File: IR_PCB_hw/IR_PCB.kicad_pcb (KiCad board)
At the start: 4 copper layers, 49.5 x 49 mm, 130 parts, among them Q1 M28S, Q10 SI2303, Q11 SI2303, Q2 M28S, Q3 TSOP48xx, Q4 TSOP48xx, Q5 SI2303, Q6 TSOP48xx, Q7 SI2303, Q8 SI2303, Q9 SI2303

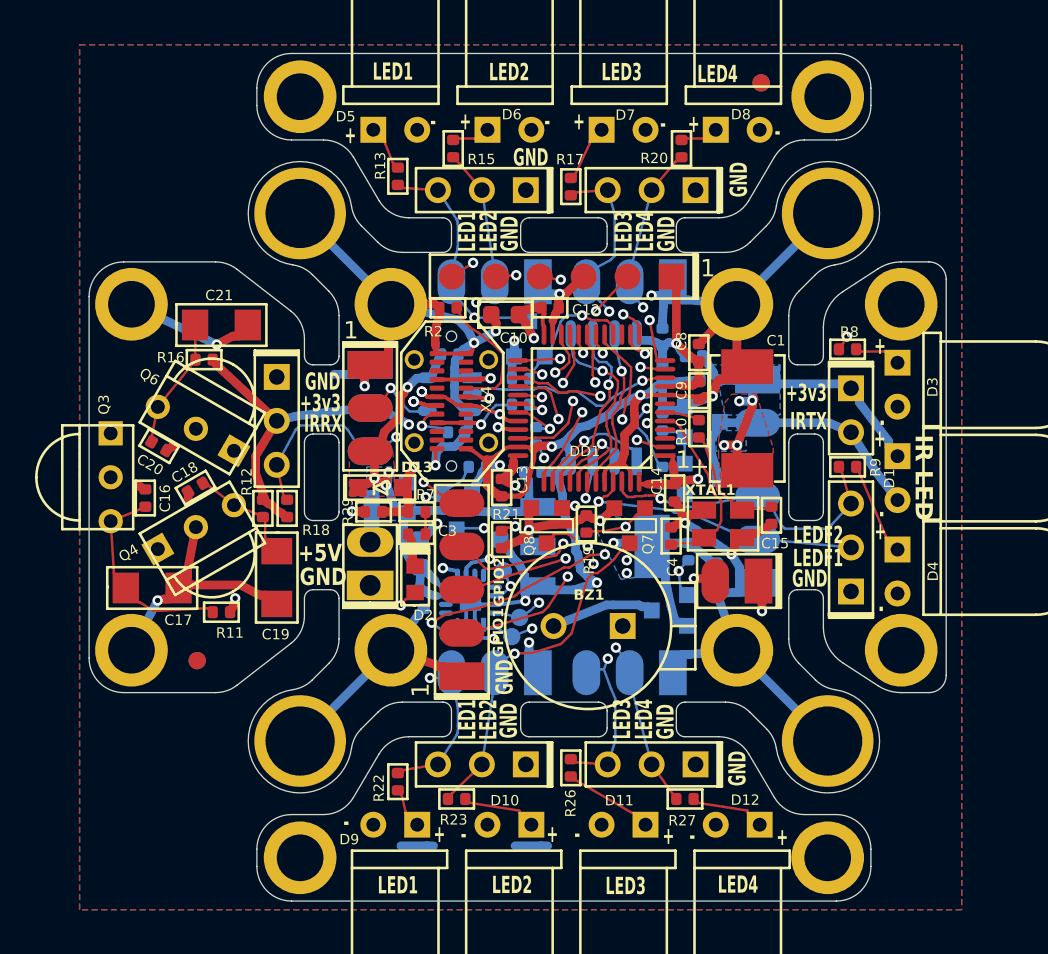
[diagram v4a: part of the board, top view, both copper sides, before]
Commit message: Replace USB conn with micro one Replace 0402 wit 0603
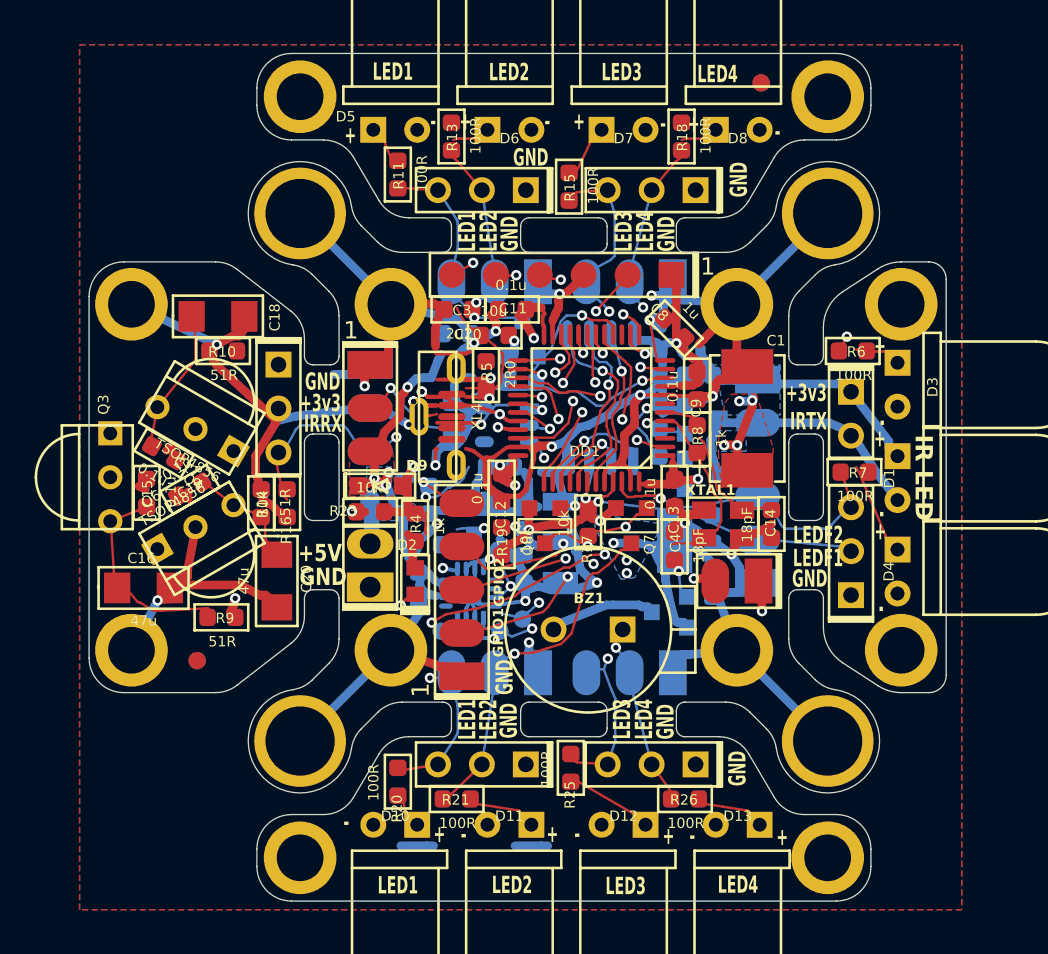
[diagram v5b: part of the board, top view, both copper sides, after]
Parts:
- removed the C15 at (152.0, 111.2)
- removed the C17 at (116.2, 115.4)
- removed the C21 at (120.2, 100.2)
- removed the C23 at (131.7, 113.4)
- removed C26: 10u, Capacitors:CAP_0603_Fab
- removed the D9 at (130.2, 129.1)
- removed the R2 at (133.3, 99.2)
- removed the R3 at (133.8, 106.4)
- added C14: 18pF, Capacitors:CAP_0603_Silks, F.Cu at (152.0, 111.7)
- added C16: 47u, Capacitors:CAP_1206, F.Cu at (115.7, 115.4)
- added C20: 47u, Capacitors:CAP_1206, F.Cu at (123.4, 115.0)
- added C22: 10u, Capacitors:CAP_0603_Silks, B.Cu at (132.1, 112.9)
- added C24: 10u, Capacitors:CAP_0603_Silks, B.Cu at (132.2, 110.3)
- added D13: ~, LEDs:LED5mmR, F.Cu at (150.1, 129.1)
- BZ1: value PS-9627 -> 9650-5.5R/16R
- C1: value 470uF -> 330uF
- C10, C25: footprint Capacitors:CAP_0603_Fab -> Capacitors:CAP_0603_Silks
- C11: renamed from C12; footprint Capacitors:CAP_0402_Fab -> Capacitors:CAP_0603_Silks
- C12: renamed from C13; footprint Capacitors:CAP_0402_Fab -> Capacitors:CAP_0603_Silks
- C13: renamed from C14; footprint Capacitors:CAP_0402_Fab -> Capacitors:CAP_0603_Silks
- C15: renamed from C16; footprint Capacitors:CAP_0402_Fab -> Capacitors:CAP_0603_Silks
- C17: renamed from C18; footprint Capacitors:CAP_0402_Fab -> Capacitors:CAP_0603_Silks
- C19: renamed from C20; footprint Capacitors:CAP_0402_Fab -> Capacitors:CAP_0603_Silks
- C2, C3, C4, C5, C6, C7, C8, C9: footprint Capacitors:CAP_0402_Fab -> Capacitors:CAP_0603_Silks
- C21: renamed from C22; footprint Capacitors:CAP_0402_Fab -> Capacitors:CAP_0603_Silks
- C23: renamed from C24; footprint Capacitors:CAP_0402_Fab -> Capacitors:CAP_0603_Silks
- D10, D11, D12, D5, D6, D7, D8: value BL-L502URC -> ~
- D2: value L-C191LBCT -> LTST-C191KGKT
- D3, D4: value BL-L522PGC -> ~
- DD2: value W25Q32JV -> W25Q32JVSIQ
- Q10: renamed from Q9; value SI2303 -> SI2301
- Q11, Q5, Q7, Q8: value SI2303 -> SI2301
- Q3, Q4, Q6: value TSOP48xx -> TSOP4856
- Q9: renamed from Q10; value SI2303 -> SI2301
- R1: footprint Resistors:RES_0402_Fab -> Resistors:RES_0603_Silks
- R10: renamed from R12; footprint Resistors:RES_0402_Fab -> Resistors:RES_0603_Silks
- R11: renamed from R13; footprint Resistors:RES_0402_Fab -> Resistors:RES_0603_Silks
- R12: renamed from R14; footprint Resistors:RES_0402_Fab -> Resistors:RES_0603_Silks
- R13: renamed from R15; footprint Resistors:RES_0402_Fab -> Resistors:RES_0603_Silks
- R14: renamed from R16; footprint Resistors:RES_0402_Fab -> Resistors:RES_0603_Silks
- R15: renamed from R17; footprint Resistors:RES_0402_Fab -> Resistors:RES_0603_Silks
- R16: renamed from R18; footprint Resistors:RES_0402_Fab -> Resistors:RES_0603_Silks
- R17: renamed from R19; footprint Resistors:RES_0402_Fab -> Resistors:RES_0603_Silks
- R18: renamed from R20; footprint Resistors:RES_0402_Fab -> Resistors:RES_0603_Silks
- R19: renamed from R21; footprint Resistors:RES_0402_Fab -> Resistors:RES_0603_Silks
- R2: renamed from R4; footprint Resistors:RES_0402_Fab -> Resistors:RES_0603_Silks
- R20: renamed from R22; footprint Resistors:RES_0402_Fab -> Resistors:RES_0603_Silks
- R21: renamed from R23; footprint Resistors:RES_0402_Fab -> Resistors:RES_0603_Silks
- R22: renamed from R24; footprint Resistors:RES_0402_Fab -> Resistors:RES_0603_Silks
- R23: renamed from R29; footprint Resistors:RES_0402_Fab -> Resistors:RES_0603_Silks
- R24: renamed from R25; footprint Resistors:RES_0402_Fab -> Resistors:RES_0603_Silks
- R25: renamed from R26; footprint Resistors:RES_0402_Fab -> Resistors:RES_0603_Silks
- R26: renamed from R27; footprint Resistors:RES_0402_Fab -> Resistors:RES_0603_Silks
- R3: renamed from R5; footprint Resistors:RES_0402_Fab -> Resistors:RES_0603_Silks
- R4: renamed from R6; footprint Resistors:RES_0402_Fab -> Resistors:RES_0603_Silks; moved to F.Cu
- R5: renamed from R7; footprint Resistors:RES_0402_Fab -> Resistors:RES_0603_Silks
- R6: renamed from R8; footprint Resistors:RES_0402_Fab -> Resistors:RES_0603_Silks
- R7: renamed from R9; footprint Resistors:RES_0402_Fab -> Resistors:RES_0603_Silks
- R8: renamed from R10; footprint Resistors:RES_0402_Fab -> Resistors:RES_0603_Silks
- R9: renamed from R11; footprint Resistors:RES_0402_Fab -> Resistors:RES_0603_Silks
- XL4: value USB_C -> DS1105-11; footprint Connectors:USBC_24PF-009 -> Connectors:USBmicro_Connfly_DS1105-11
- moved C18 15.5 mm to (120.0, 99.7), turned to 0 degrees
- moved C3 13.2 mm to (133.9, 99.3), turned to 0 degrees
- moved R10 9.39 mm to (120.3, 101.7), turned to 0 degrees
- moved R14 8.93 mm to (122.5, 110.5), turned to 90 degrees
- moved R5 8.85 mm to (135.5, 103.1), turned to 90 degrees
- moved R4 8.78 mm to (131.4, 111.9)
- moved D12 6.60 mm to (143.4, 129.1)
- moved D10 6.60 mm to (130.2, 129.1)
- moved D11 6.60 mm to (136.8, 129.1)
- moved Q6 5.68 mm to (118.7, 111.9), turned to 30 degrees
- moved Q4 5.67 mm to (118.7, 106.2), turned to 150 degrees
- moved R1 4.24 mm to (148.6, 112.0)
- moved R3 4.06 mm to (133.5, 105.5), turned to 90 degrees
- moved DA1 3.76 mm to (136.7, 106.0)
- moved C19 3.07 mm to (118.4, 109.7), turned to -150 degrees
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- renumbered C19 to C18, D13 to D9, TP2 to TP1, TP3 to TP2, TP4 to TP3, TP5 to TP4, XL14 to XL10, XL15 to XL11, XL16 to XL12, XL17 to XL13, XL18 to XL14, XL19 to XL15, XL20 to XL16, XL21 to XL17, XL22 to XL18, XL23 to XL19, XL24 to XL20, XL7 to XL6, XL8 to XL7, XL9 to XL8, XL10 to XL9
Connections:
- C25 pad 1: +PwrUnst -> +3v3
- R20 pad 2: Net-(D9-PadA) -> Net-(D10-PadA)
- R21 pad 2: Net-(D10-PadA) -> Net-(D11-PadA)
- R25 pad 2: Net-(D11-PadA) -> Net-(D12-PadA)
- R26 pad 2: Net-(D12-PadA) -> Net-(D13-PadA)
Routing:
- net (no net): track 0.00 -> 17.4 mm, vias 0 -> 1
- net Net-(D2-PadA): track 14.1 -> 1.93 mm, vias 2 -> 0
- net GND: track 281.7 -> 293.8 mm, vias 19 -> 21
- net /USB_CC1: track 7.66 -> 0.00 mm
- net Net-(C14-Pad1): track 6.89 -> 0.00 mm
- net Net-(D13-PadA): track 0.00 -> 4.33 mm
- net /USB_CC2: track 2.83 -> 0.00 mm, vias 1 -> 0
- net Net-(D9-PadA): track 2.37 -> 0.00 mm
- net Net-(D10-PadA): track 4.33 -> 2.37 mm
- net Net-(Q6-Vs): track 7.55 -> 6.30 mm
- net Net-(Q4-Vs): track 6.30 -> 7.55 mm
- net Net-(D12-PadA): track 4.33 -> 5.18 mm
- net Net-(D11-PadA): track 5.18 -> 4.33 mm

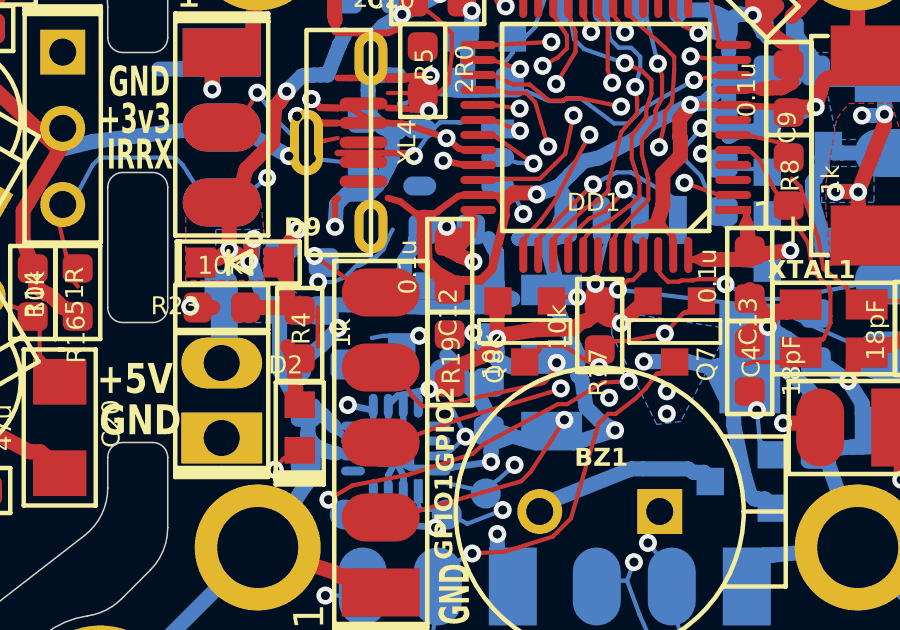
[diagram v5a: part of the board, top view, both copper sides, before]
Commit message: RTOS, UART, XTAL work
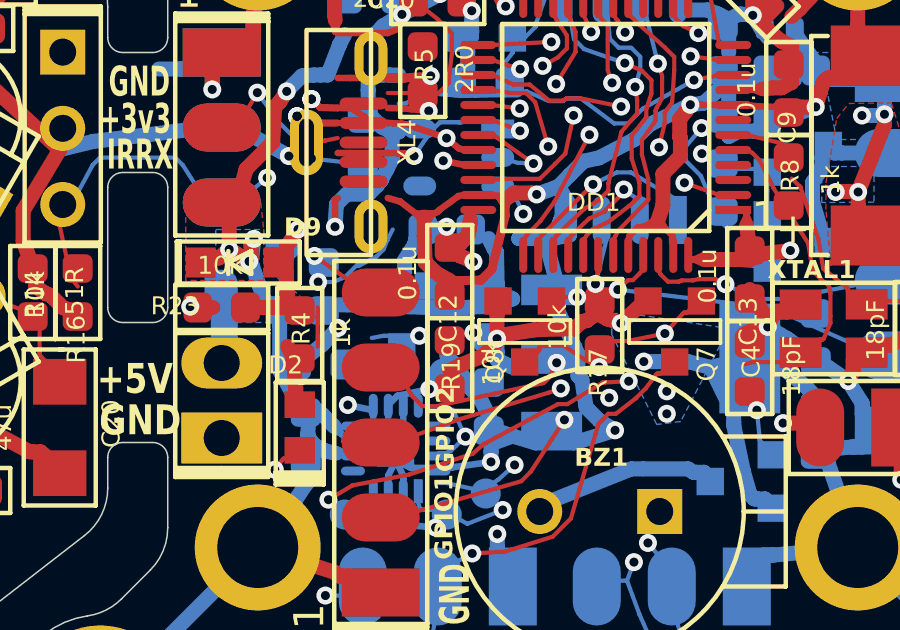
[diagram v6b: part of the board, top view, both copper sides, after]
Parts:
- moved C12 0.20 mm to (136.4, 109.8)
- moved R19 0.20 mm to (136.4, 112.9)
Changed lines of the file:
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@@
   )
   (footprint "Capacitors:CAP_0603_Silks" (layer "F.Cu")
-    (at 136.4 109.6 -90)
+    (at 136.4 109.8 -90)
     (property "Description" "X5R or X7R capacitor, 6.3V or higher")
     (property "Dielectric" "X5R or X7R")
@@
   )
   (footprint "Resistors:RES_0603_Silks" (layer "F.Cu")
-    (at 136.4 112.7 90)
+    (at 136.4 112.9 90)
     (property "Description" "1% resistor")
     (property "PN" "-")

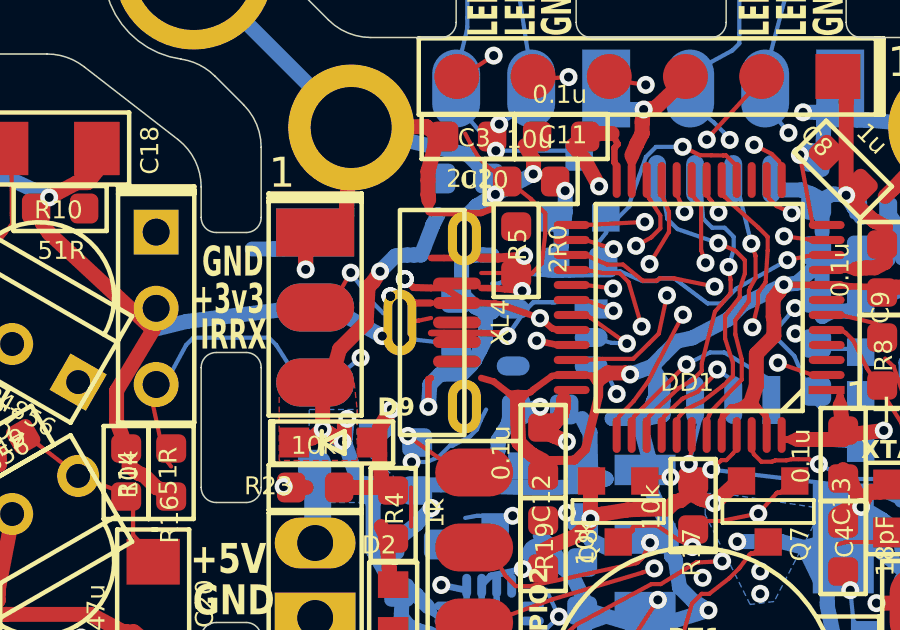
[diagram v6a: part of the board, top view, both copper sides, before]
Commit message: Usb conn moved
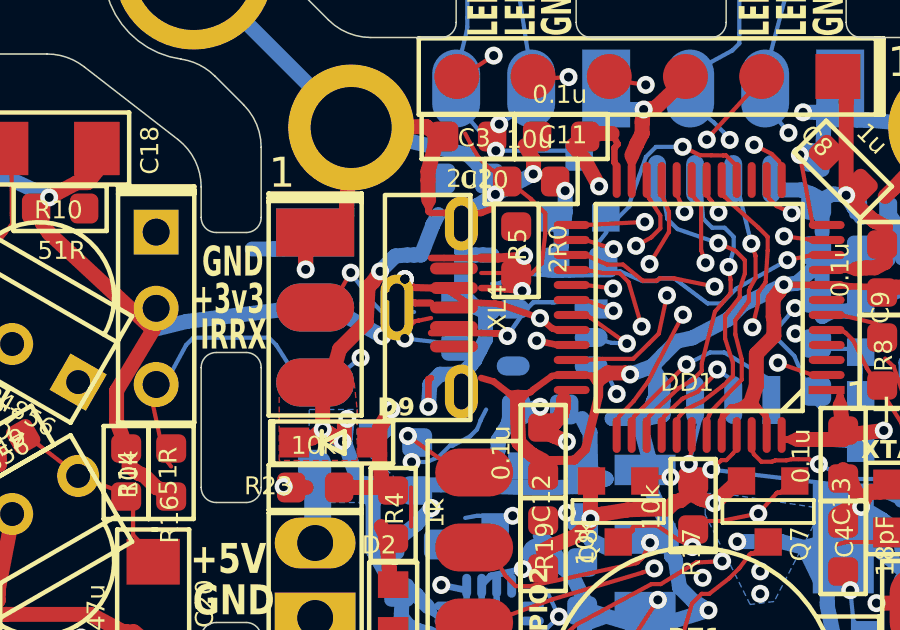
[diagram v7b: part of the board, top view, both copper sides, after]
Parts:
- moved XL4 0.51 mm to (133.7, 105.0)
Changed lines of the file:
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@@
   )
   (footprint "Connectors:USBmicro_Connfly_DS1105-11" (layer "F.Cu")
-    (at 133.775 105.5 -90)
+    (at 133.675 105 -90)
     (property "PN" "DS1105-11-05SS8BNRS")
     (property "Price" "49")
@@
         (effects (font (size 0.6 0.6) (thickness 0.15)))
     )
-    (fp_rect (start -3.75 0) (end 3.75 2.15)
+    (fp_rect (start -3.75 -0.3) (end 3.75 2.55)
       (stroke (width 0.15) (type default)) (fill none) (layer "F.SilkS"))
     (pad "1" smd oval (at -1.3 0.25 270) (size 0.4 1.6) (layers "F.Cu" "F.Paste" "F.Mask")
@@
     (pad "H3" thru_hole oval (at 0 2.15 270) (size 2.2 1.1) (drill oval 1.6 0.5) (layers "*.Cu" "*.Mask")
       (net 75 "unconnected-(XL4-PadH3)") (pintype "passive+no_connect"))
-    (model "${KICAD_SYMBOL_DIR}/3d/Connectors/molex_1050170001.STEP"
-      (offset (xyz 0 1.65 1.1))
+    (model ":KICAD7_3DMODEL_DIR:Connectors/uUsb-5P-H63.stp"
+      (offset (xyz 14.72 -2.77 21.3))
       (scale (xyz 1 1 1))
-      (rotate (xyz -90 0 0))
+      (rotate (xyz 90 -180 0))
     )
   )

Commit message: PCB v3.2 Routing done, cleanup done
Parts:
- moved TP3 3.10 mm to (137.1, 116.2)
- moved C5 2.43 mm to (135.2, 102.7), turned to 90 degrees
- moved TP2 0.68 mm to (136.9, 118.3)
- moved R3 0.55 mm to (133.4, 105.0), turned to -90 degrees
- moved TP1 0.52 mm to (138.1, 116.9)
- moved Q7 0.33 mm to (144.0, 112.1)
- moved R23 0.31 mm to (129.1, 111.0)
- moved C7 0.24 mm to (145.7, 100.8)
- moved C22 0.22 mm to (132.3, 112.9)
- moved L1 0.21 mm to (147.6, 101.7)
- moved DA1 0.20 mm to (136.5, 106.0)
- moved R19 0.14 mm to (136.5, 113.0)
- moved Q11 0.12 mm to (134.7, 111.4)
- moved R24 0.11 mm to (136.4, 108.4)
- moved DD2 0.07 mm to (142.1, 104.5)
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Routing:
- net (no net): track 17.4 -> 0.00 mm, vias 1 -> 0
- net GND: track 293.8 -> 277.8 mm, vias 21 -> 77
- net /USB_D+: track 12.4 -> 4.23 mm, vias 4 -> 0
- net Net-(DD1-PA10): track 2.94 -> 11.0 mm, vias 1 -> 2
- net /USB_D-: track 11.7 -> 4.28 mm, vias 3 -> 0
- net +5vUSB: track 21.2 -> 14.4 mm, vias 3 -> 2
- net Net-(C14-Pad1): track 0.00 -> 6.22 mm
- net Net-(DD1-PA9): track 2.29 -> 7.52 mm, vias 1 -> 2
- net Net-(Q6-Vs): track 6.30 -> 11.2 mm
- net /NPX_DATA: track 4.62 -> 8.60 mm, vias 1 -> 2
- net +3v3: track 111.5 -> 115.3 mm, vias 13 -> 15
- net +PwrMCU: track 56.3 -> 59.9 mm
- net /Gpio4: track 13.0 -> 9.81 mm
- net /LED_PWM4_IN: track 18.6 -> 15.5 mm
- net /IR_RCVR: track 47.6 -> 44.6 mm
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- added copper zone on F.Cu, net +PwrMCU
